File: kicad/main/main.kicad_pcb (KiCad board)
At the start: 2 copper layers, 170 x 110 mm, 122 parts, among them J1 USB_C_Receptacle_USB2.0, J10 drib-kick, J11 drib-kick, J12 LINE, J13 ICSP, J14 MD1, J15 MD2, J16 MD3, J17 MD4, J18 I2C/OLED, J19 ICSP, J2 I2C_2, J20 Trimmer, J21 GND-Test, J3 Power IN, J4 MD1, J5 MD2, J6 Serial0/XBee, J7 Serial1/IMU, J8 to cam, J9 I2C_1, Q1 AO3400A, Q2 AO3401A, SW1 BOOTSET, SW2 IMU SET, SW3 Reset, SW4 RESET, SW5 GOAL, SW6 START, SW7 AUX1, U1 RP2040_Stamp, U2 74HC32, U3 74HC04, U4 OKL-T_3-W12N-C, U5 ATmega328P-AU, U6 ATmega328P-AU, U7 AZ1117CH-3.3, U8 PCF8574PW, Y1 8Mhz, Y2 8Mhz

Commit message: fix: main 配線前
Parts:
- J14, J15, J16, J17: footprint 0.main.robot:JSTB4B-ZR -> 0.main.robot:JSTS4B-ZRLFSN
- moved J21 15.0 mm to (135.0, 145.0)
- moved R27 14.3 mm to (102.5, 103.5)
- moved J8 12.7 mm to (127.0, 103.8), turned to -90 degrees
- moved JP2 12.7 mm to (85.0, 85.3)
- moved J18 11.1 mm to (109.5, 102.2), turned to -90 degrees
- moved R31 9.22 mm to (209.0, 82.0)
- moved R8 8.73 mm to (130.5, 93.0), turned to -90 degrees
- moved JP1 8.59 mm to (135.0, 140.0), turned to 90 degrees
- moved R32 8.54 mm to (209.0, 88.0)
- moved C13 8.52 mm to (99.5, 97.4)
- moved D17 8.52 mm to (96.5, 97.4)
- moved R42 8.52 mm to (96.5, 101.4)
- moved R43 8.07 mm to (190.0, 65.0), turned to 180 degrees
- moved J20 8.05 mm to (133.8, 77.5), turned to 180 degrees
- moved R28 6.05 mm to (102.6, 98.5)
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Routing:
- net SW1_6: track 791.8 -> 269.6 mm, vias 7 -> 4
- net SW1_3: track 286.3 -> 0.00 mm, vias 3 -> 0
- net +5V: track 252.4 -> 0.00 mm, vias 4 -> 0
- net Vcc1: track 189.2 -> 0.00 mm, vias 4 -> 0
- net LINE_D_1: track 164.8 -> 0.00 mm, vias 3 -> 0
- net LINE_D_6: track 159.3 -> 0.00 mm, vias 3 -> 0
- net LINE_D_2: track 151.4 -> 0.00 mm, vias 4 -> 0
- net Net-(J10-Pad1): track 150.2 -> 0.00 mm, vias 1 -> 0
- net LINE_D_5: track 148.7 -> 0.00 mm, vias 3 -> 0
- net LINE_D_3: track 142.4 -> 0.00 mm, vias 2 -> 0
- net LINE_D_4: track 140.0 -> 0.00 mm, vias 3 -> 0
- net Net-(C11-Pad1): track 133.8 -> 0.00 mm, vias 2 -> 0
- net I2C_1.SDA: track 125.8 -> 0.00 mm, vias 2 -> 0
- net I2C_1.SCL: track 124.9 -> 0.00 mm, vias 1 -> 0
- net Net-(J12-Pad3): track 118.3 -> 0.00 mm
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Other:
- board size 170 x 110 mm -> 170 x 100 mm

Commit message: fix
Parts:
- moved C6 23.1 mm to (121.5, 146.8), turned to 0 degrees
- moved D9 18.9 mm to (118.0, 143.1), turned to -90 degrees
- moved R24 18.7 mm to (127.0, 143.0), turned to -90 degrees
- moved R25 17.9 mm to (120.9, 143.1), turned to 90 degrees
- moved D8 17.7 mm to (124.0, 143.0), turned to -90 degrees
- moved Y1 15.0 mm to (112.0, 131.6), turned to -90 degrees
- moved C5 10.9 mm to (130.0, 135.1), turned to -90 degrees
- moved D6 6.66 mm to (121.0, 135.0), turned to 90 degrees
- moved U5 6.66 mm to (121.0, 135.0), turned to 0 degrees
- moved J13 6.54 mm to (123.8, 123.5), turned to 0 degrees
- moved R26 5.43 mm to (117.9, 78.5)
- moved D10 5.00 mm to (102.0, 78.0), turned to -90 degrees
- moved C7 4.84 mm to (118.0, 81.0)
- moved C8 4.84 mm to (118.0, 84.0)
- moved Y2 4.73 mm to (115.5, 88.7)
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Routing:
- net SW1_6: track 269.6 -> 212.3 mm, vias 4 -> 0
- net +15V: track 229.8 -> 224.8 mm, vias 4 -> 0

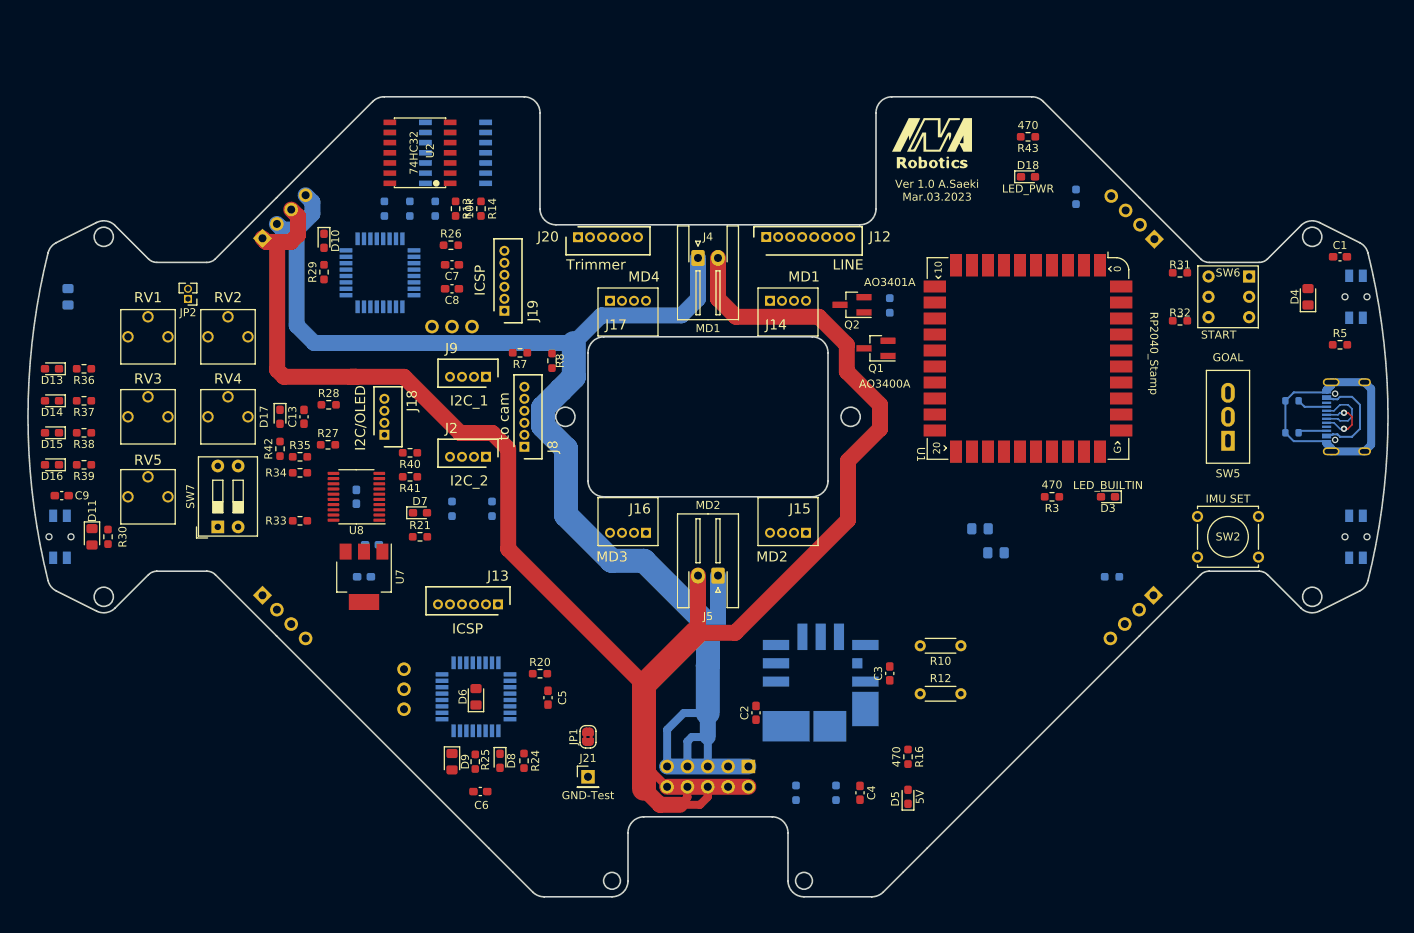
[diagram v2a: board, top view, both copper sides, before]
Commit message: 未配線　２か所
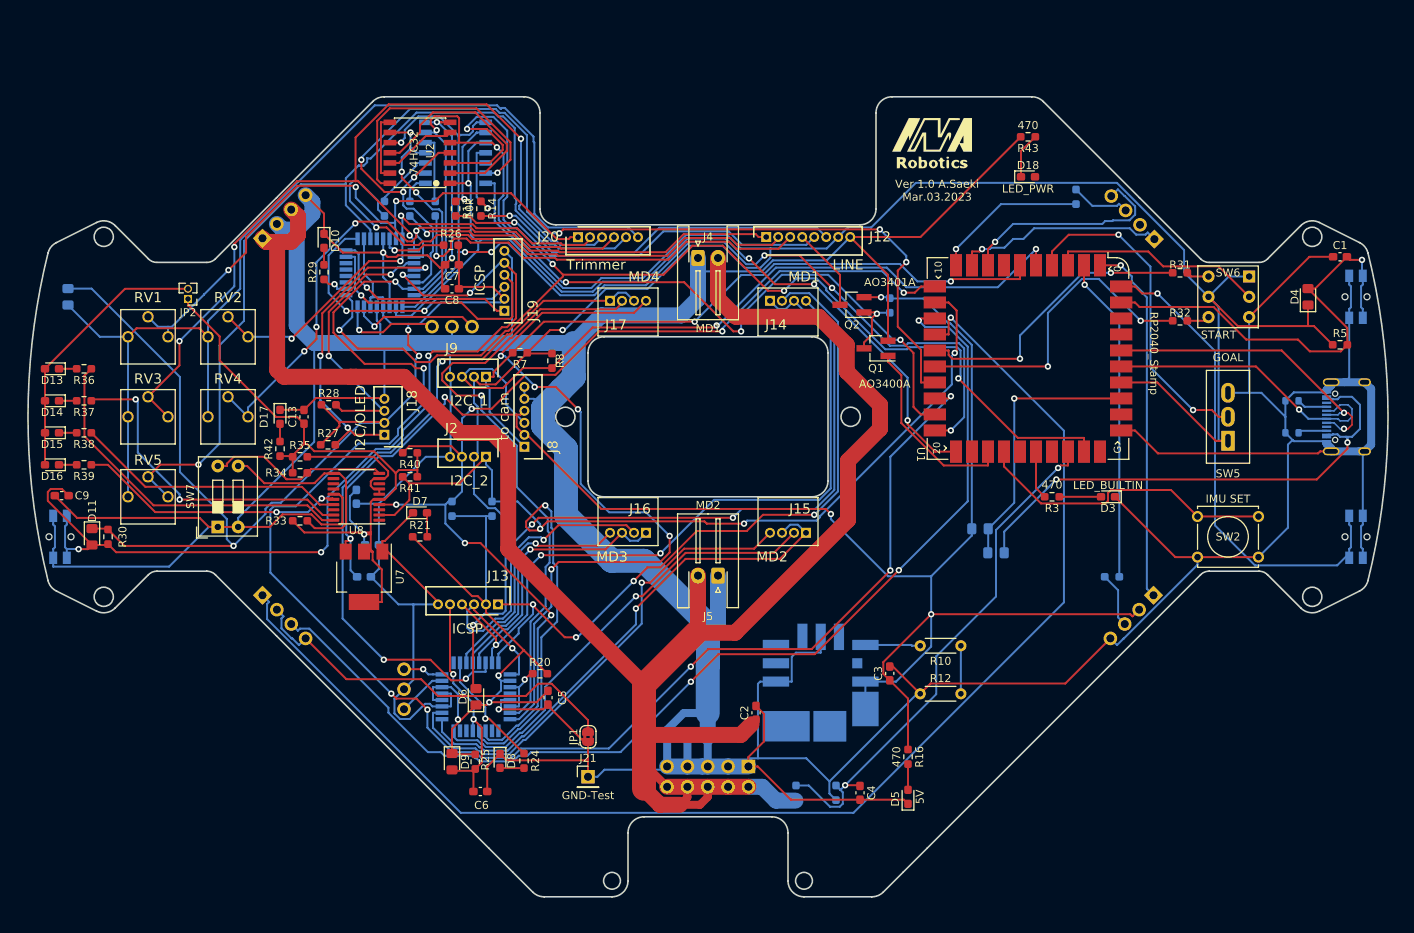
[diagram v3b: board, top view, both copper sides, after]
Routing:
- net SW1_6: track 212.3 -> 876.7 mm, vias 0 -> 4
- net SW1_3: track 0.00 -> 271.1 mm, vias 0 -> 2
- net +5V: track 0.00 -> 220.0 mm, vias 0 -> 5
- net LINE_D_2: track 0.00 -> 219.6 mm, vias 0 -> 10
- net Net-(J10-Pad1): track 0.00 -> 169.4 mm, vias 0 -> 1
- net LINE_D_6: track 0.00 -> 163.3 mm, vias 0 -> 5
- net Vcc1: track 0.00 -> 155.5 mm, vias 0 -> 3
- net I2C_1.SCL: track 0.00 -> 147.7 mm, vias 0 -> 4
- net I2C_1.SDA: track 0.00 -> 138.5 mm, vias 0 -> 6
- net LINE_D_1: track 0.00 -> 136.3 mm, vias 0 -> 6
- net Net-(J10-Pad3): track 0.00 -> 134.6 mm, vias 0 -> 3
- net Net-(D12-Pad2): track 0.00 -> 133.0 mm
- net LINE_D_4: track 0.00 -> 130.1 mm, vias 0 -> 6
- net LINE_D_3: track 0.00 -> 124.5 mm, vias 0 -> 5
- net Net-(C9-Pad1): track 0.00 -> 118.5 mm, vias 0 -> 5
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
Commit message: fix: 配線後
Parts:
- added R44: 10k, Resistor_SMD:R_0603_1608Metric_Pad0.98x0.95mm_HandSolder, F.Cu at (196.8, 76.2)
- C2, JP1: moved to B.Cu
- moved JP1 49.5 mm to (128.2, 90.9), turned to 180 degrees
- moved R11 17.7 mm to (124.5, 64.5)
- moved R9 17.6 mm to (127.5, 64.5)
- moved R15 13.8 mm to (126.0, 64.5)
- moved R12 10.2 mm to (176.8, 124.5)
- moved C3 3.68 mm to (174.0, 128.6)
- moved C2 3.51 mm to (154.4, 133.9)
- moved R19 0.65 mm to (165.4, 147.1), turned to 90 degrees
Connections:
- J10 pad 2: Net-(J10-Pad2) -> SW1_6
- J10 pad 4: Net-(J10-Pad2) -> SW1_6
- J11 pad 2: SW1_6 -> Net-(J11-Pad2)
- J11 pad 4: SW1_6 -> Net-(J11-Pad2)
- JP1 pad 2: Net-(J10-Pad2) -> Net-(J11-Pad2)
- U1 pad 8: Net-(J7-Pad4) -> Net-(U1-Pad8)
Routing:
- net Net-(J12-Pad5): track 49.6 -> 205.0 mm, vias 1 -> 12
- net LINE_D_2: track 219.6 -> 109.1 mm, vias 10 -> 5
- net LINE_D_6: track 163.3 -> 228.9 mm, vias 5 -> 4
- net +5V: track 220.0 -> 275.7 mm
- net Net-(J11-Pad2): track 0.00 -> 50.4 mm
- net Net-(J10-Pad2): track 49.2 -> 0.00 mm
- net SW1_6: track 876.7 -> 840.1 mm, vias 4 -> 5
- net I2C_1.SDA: track 138.5 -> 172.3 mm, vias 6 -> 7
- net I2C_0.SCL: track 86.4 -> 119.8 mm, vias 2 -> 4
- net Net-(J17-Pad1): track 88.9 -> 56.0 mm, vias 3 -> 1
- net Net-(J20-Pad4): track 74.3 -> 107.0 mm, vias 4 -> 3
- net Net-(J17-Pad4): track 96.2 -> 65.1 mm, vias 5 -> 1
- net Net-(J10-Pad1): track 169.4 -> 138.9 mm, vias 1 -> 4
- net Net-(J20-Pad3): track 108.5 -> 84.7 mm, vias 4 -> 2
- net Net-(J7-Pad4): track 27.4 -> 4.89 mm, vias 1 -> 0
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- added copper zone on B.Cu, net SW1_6

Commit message: fix: main 発注ファイル
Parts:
- D13: value LED1_R -> R
- D14: value LED2_G -> G
- D15: value LED3_Y -> Y
- D16: value LED4_B -> B
